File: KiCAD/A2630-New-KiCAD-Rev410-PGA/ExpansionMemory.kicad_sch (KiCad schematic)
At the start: 29 parts, among them U102 27C256, U103 27C256, U406 SDRAM(16Mx16), U407 SDRAM(16Mx16), U408 SDRAM(16Mx16), U409 SDRAM(16Mx16)

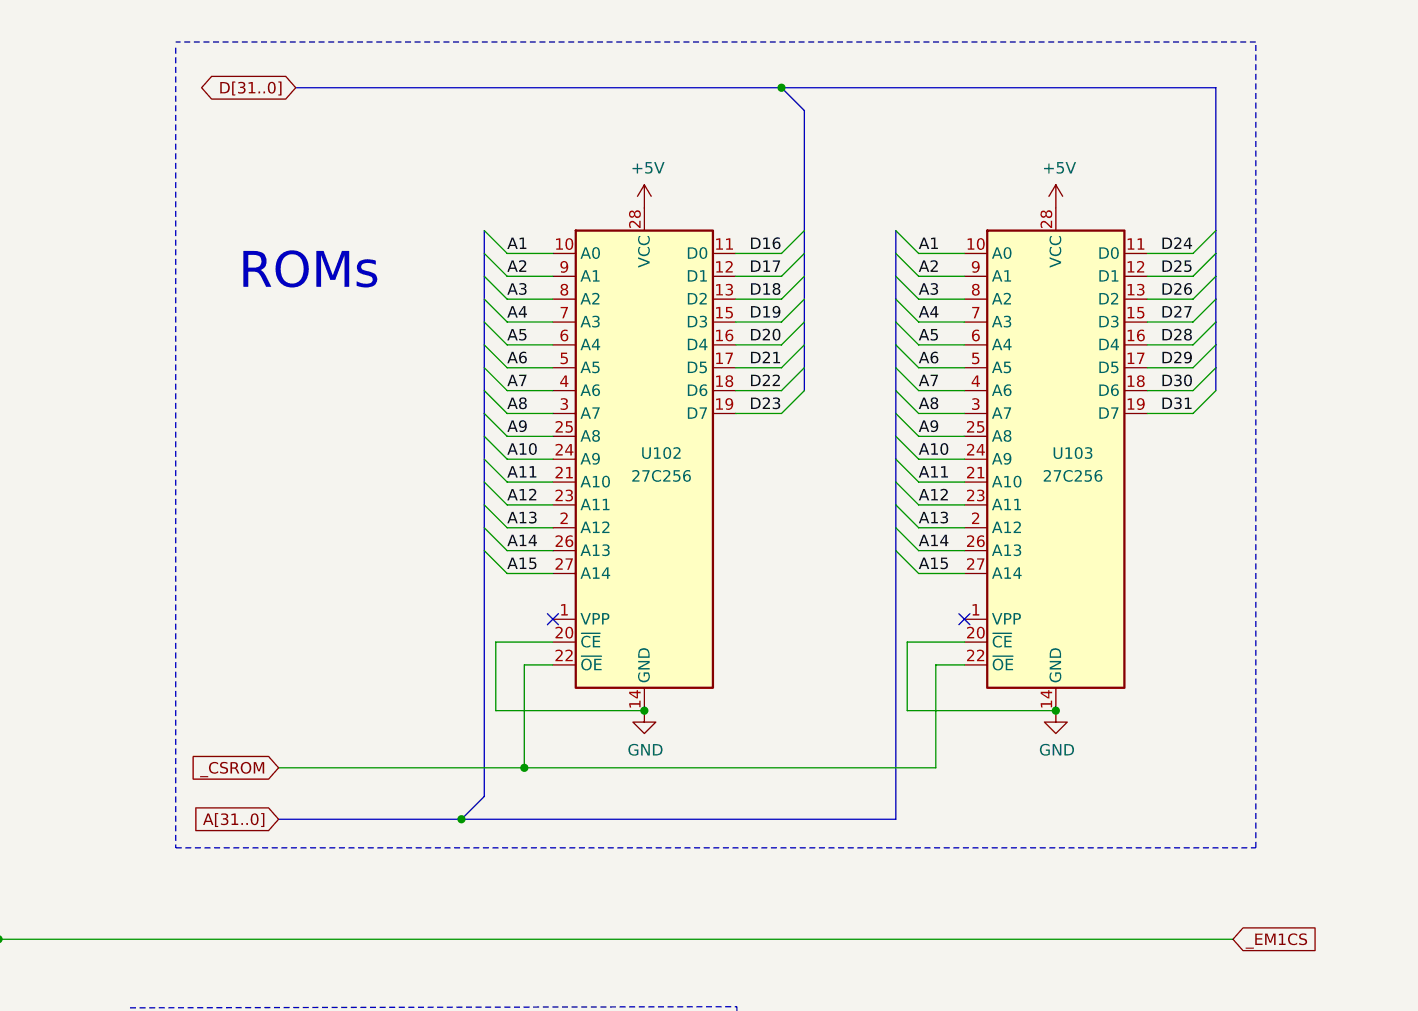
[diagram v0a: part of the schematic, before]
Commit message: Better for SMD assembly now. DRC still not done.
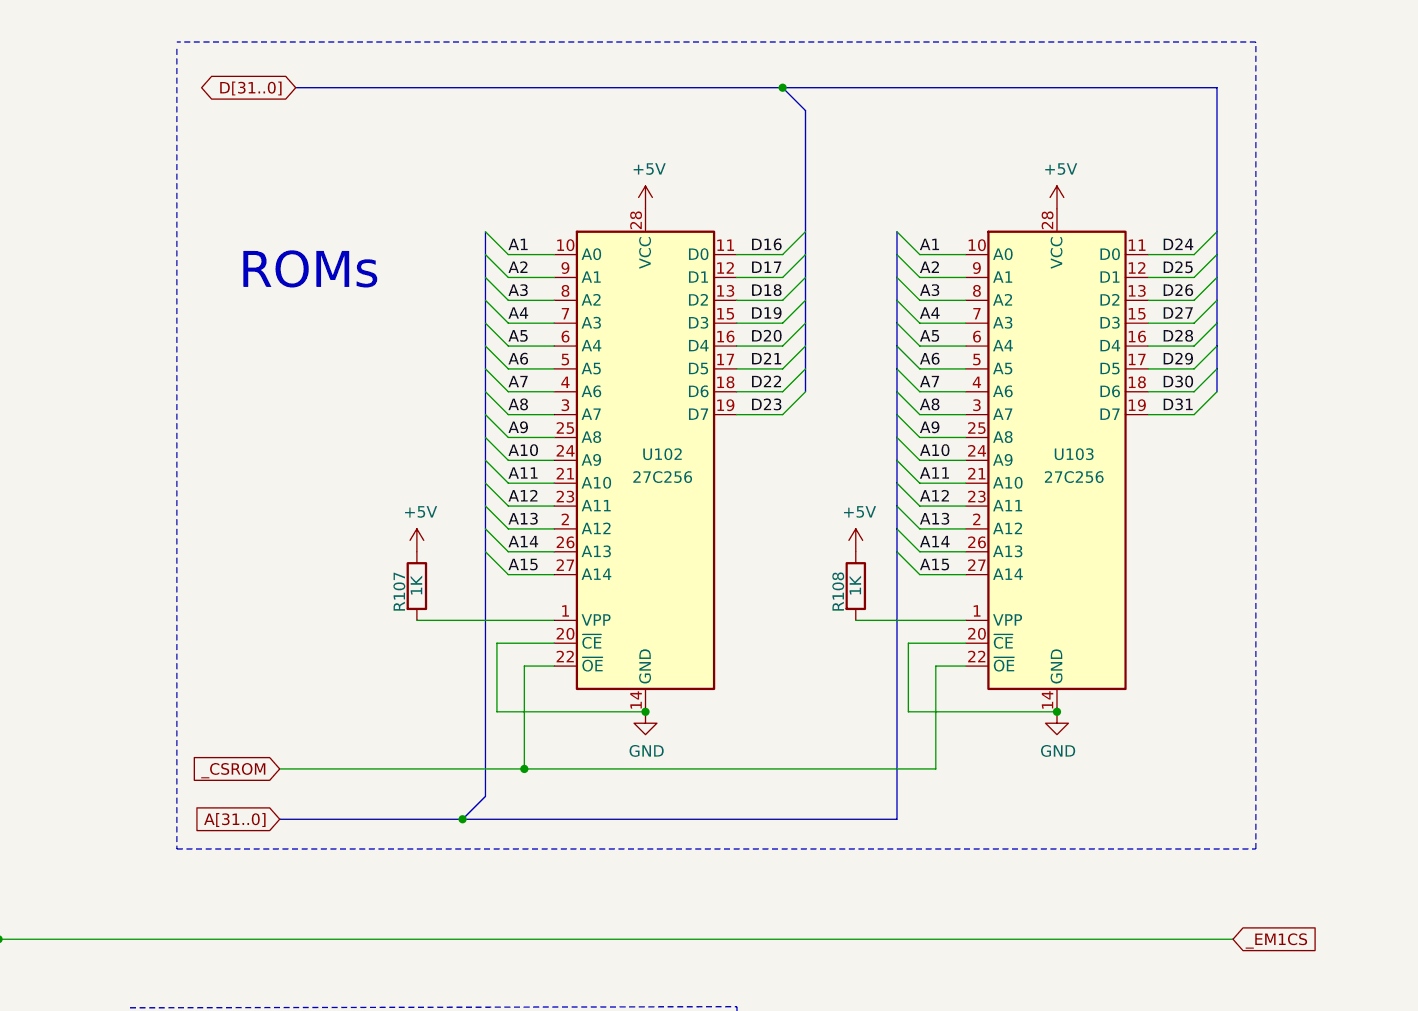
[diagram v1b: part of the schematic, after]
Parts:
- added R107, R108: 1K, Resistor_SMD:R_0805_2012Metric, symbol Device:R
- C102, C103, C406, C407, C408, C409, C410, C411, C412, C413, C422, C423, C424, C425, C426: LCSC (none) -> C49678
- R400, R401, R402, R900, R932, R933, R934: LCSC (none) -> C17513
- U406, U407, U408, U409: LCSC (none) -> C62246
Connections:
- net +5V: now also R107.1, R108.1
- net at U103.1 (VPP): now also R108.2
- net at U102.1 (VPP): now also R107.2
- no-connect marks 2 -> 0
